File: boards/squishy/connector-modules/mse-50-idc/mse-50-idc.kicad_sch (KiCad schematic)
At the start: 14 parts, among them J1 SCSI PHY Mezz, J2 Conn_02x25_Odd_Even, J3 Conn_01x04, J4 Conn_02x34_Clockwise_Shield, J5 Conn_02x24_Clockwise_Shield, U1 M24C02-RMC

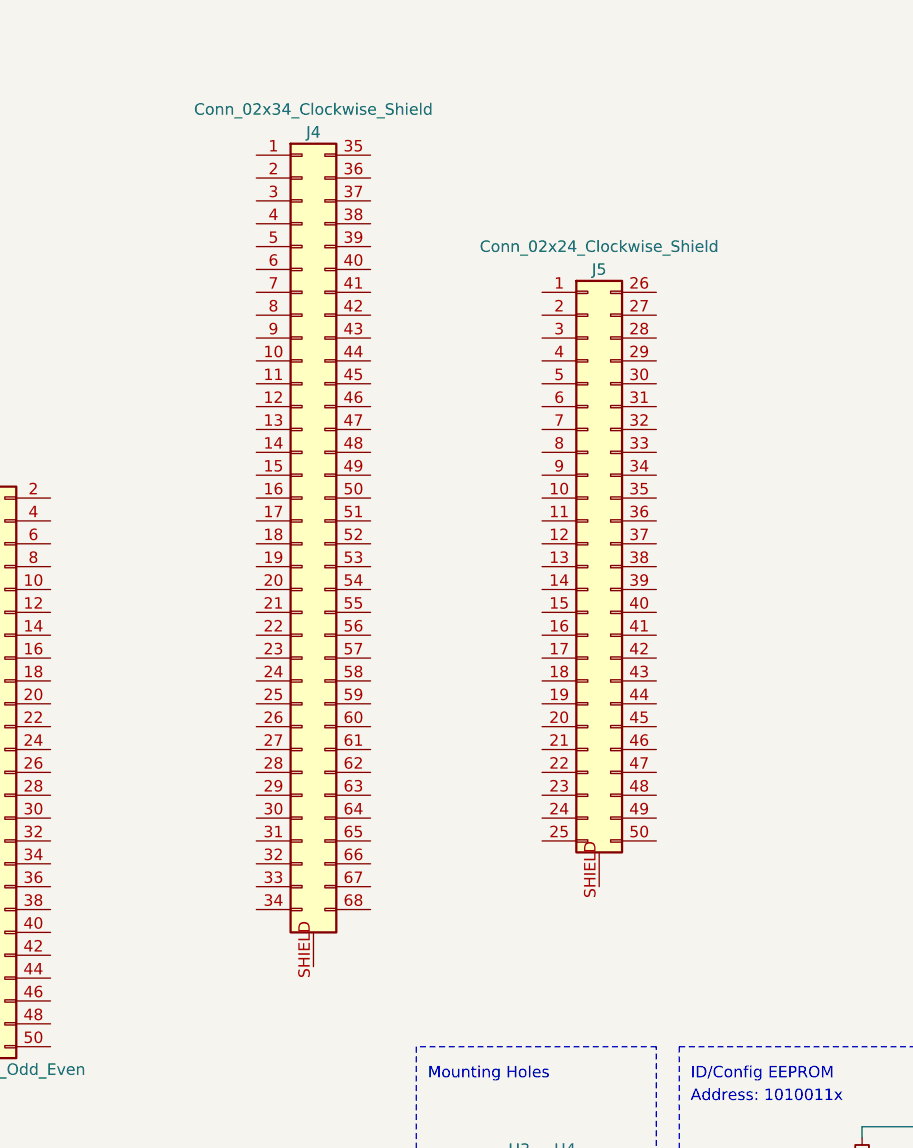
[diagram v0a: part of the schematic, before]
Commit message: squishy: connectors: Removed unneeded connector symbols in the given kicad schematics
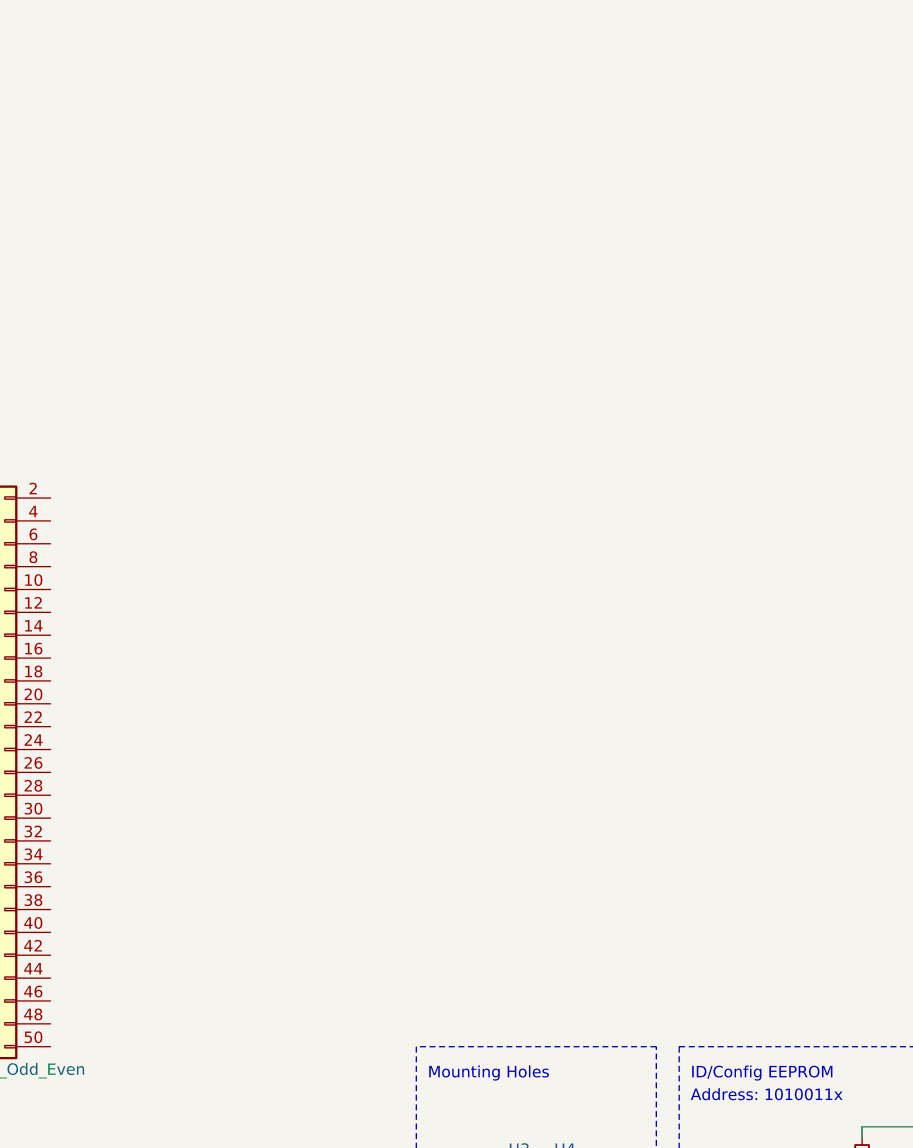
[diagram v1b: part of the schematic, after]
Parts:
- removed J4: Conn_02x34_Clockwise_Shield, symbol lethalbit-connectors:Conn_02x34_Counter_Clockwise
- removed J5: Conn_02x24_Clockwise_Shield, symbol lethalbit-connectors:Conn_02x25_Counter_Clockwise

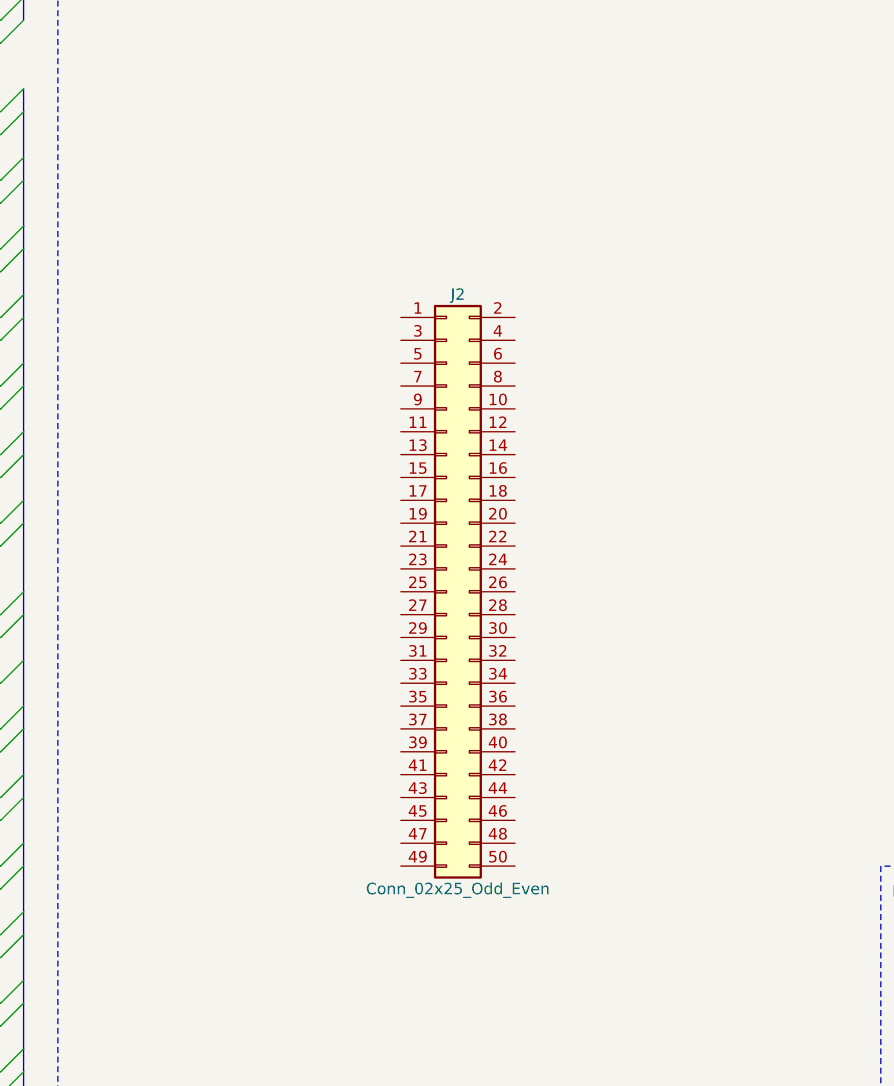
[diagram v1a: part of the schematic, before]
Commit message: squishy: connectors: hooked up mse-50-idc connector
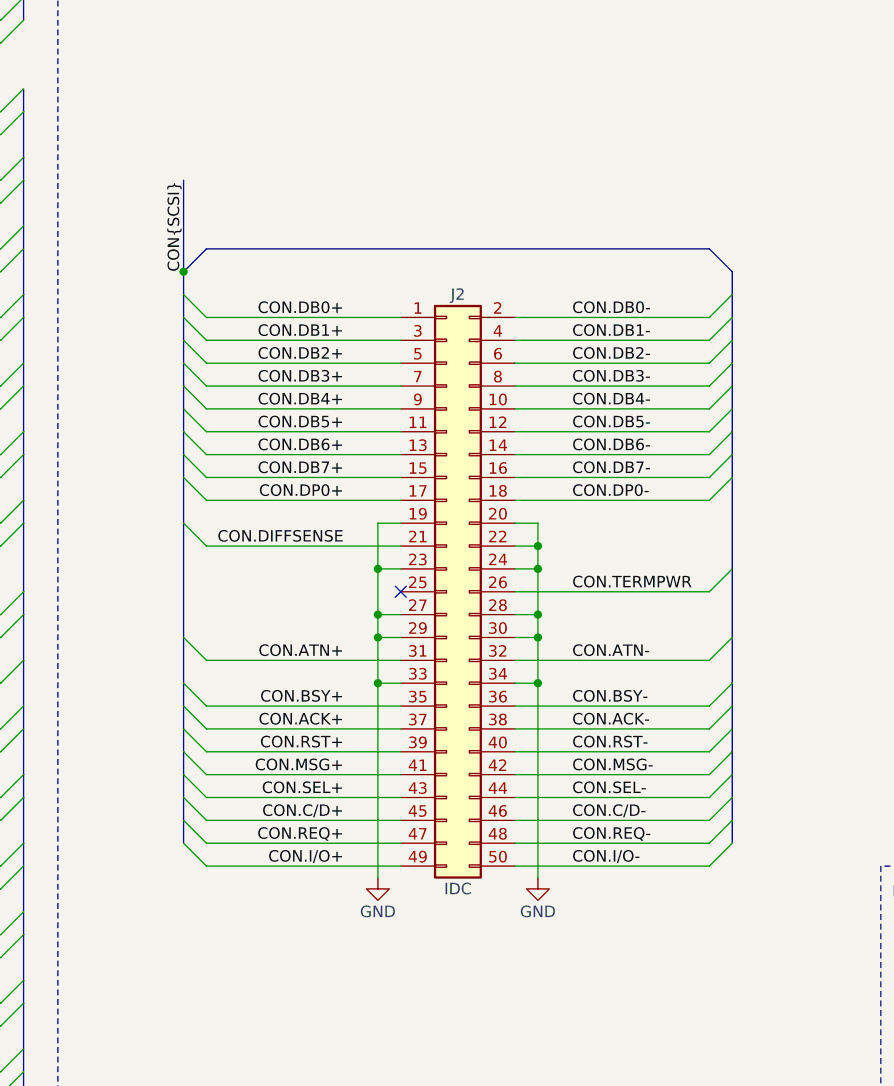
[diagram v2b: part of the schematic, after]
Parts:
- J2: value Conn_02x25_Odd_Even -> IDC
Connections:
- net CON.ACK+: now also J2.37 (Pin_37)
- net CON.ACK-: now also J2.38 (Pin_38)
- net CON.ATN+: now also J2.31 (Pin_31)
- net CON.ATN-: now also J2.32 (Pin_32)
- net CON.BSY+: now also J2.35 (Pin_35)
- net CON.BSY-: now also J2.36 (Pin_36)
- net CON.C/D+: now also J2.45 (Pin_45)
- net CON.C/D-: now also J2.46 (Pin_46)
- net CON.DB0+: now also J2.1 (Pin_1)
- net CON.DB0-: now also J2.2 (Pin_2)
- net CON.DB1+: now also J2.3 (Pin_3)
- net CON.DB1-: now also J2.4 (Pin_4)
- net CON.DB2+: now also J2.5 (Pin_5)
- net CON.DB2-: now also J2.6 (Pin_6)
- net CON.DB3+: now also J2.7 (Pin_7)
- net CON.DB3-: now also J2.8 (Pin_8)
- net CON.DB4+: now also J2.9 (Pin_9)
- net CON.DB4-: now also J2.10 (Pin_10)
- net CON.DB5+: now also J2.11 (Pin_11)
- net CON.DB5-: now also J2.12 (Pin_12)
- net CON.DB6+: now also J2.13 (Pin_13)
- net CON.DB6-: now also J2.14 (Pin_14)
- net CON.DB7+: now also J2.15 (Pin_15)
- net CON.DB7-: now also J2.16 (Pin_16)
- net CON.DIFFSENSE: now also J2.21 (Pin_21)
- net CON.DP0+: now also J2.17 (Pin_17)
- net CON.DP0-: now also J2.18 (Pin_18)
- net CON.I/O+: now also J2.49 (Pin_49)
- net CON.I/O-: now also J2.50 (Pin_50)
- net CON.MSG+: now also J2.41 (Pin_41)
- net CON.MSG-: now also J2.42 (Pin_42)
- net CON.REQ+: now also J2.47 (Pin_47)
- net CON.REQ-: now also J2.48 (Pin_48)
- net CON.RST+: now also J2.39 (Pin_39)
- net CON.RST-: now also J2.40 (Pin_40)
- net CON.SEL+: now also J2.43 (Pin_43)
- net CON.SEL-: now also J2.44 (Pin_44)
- net CON.TERMPWR: now also J2.26 (Pin_26)
- net GND: now also J2.19 (Pin_19), J2.20 (Pin_20), J2.22 (Pin_22), J2.23 (Pin_23), J2.24 (Pin_24), J2.27 (Pin_27), J2.28 (Pin_28), J2.29 (Pin_29), J2.30 (Pin_30), J2.33 (Pin_33), J2.34 (Pin_34)
- no-connect marks 2 -> 3

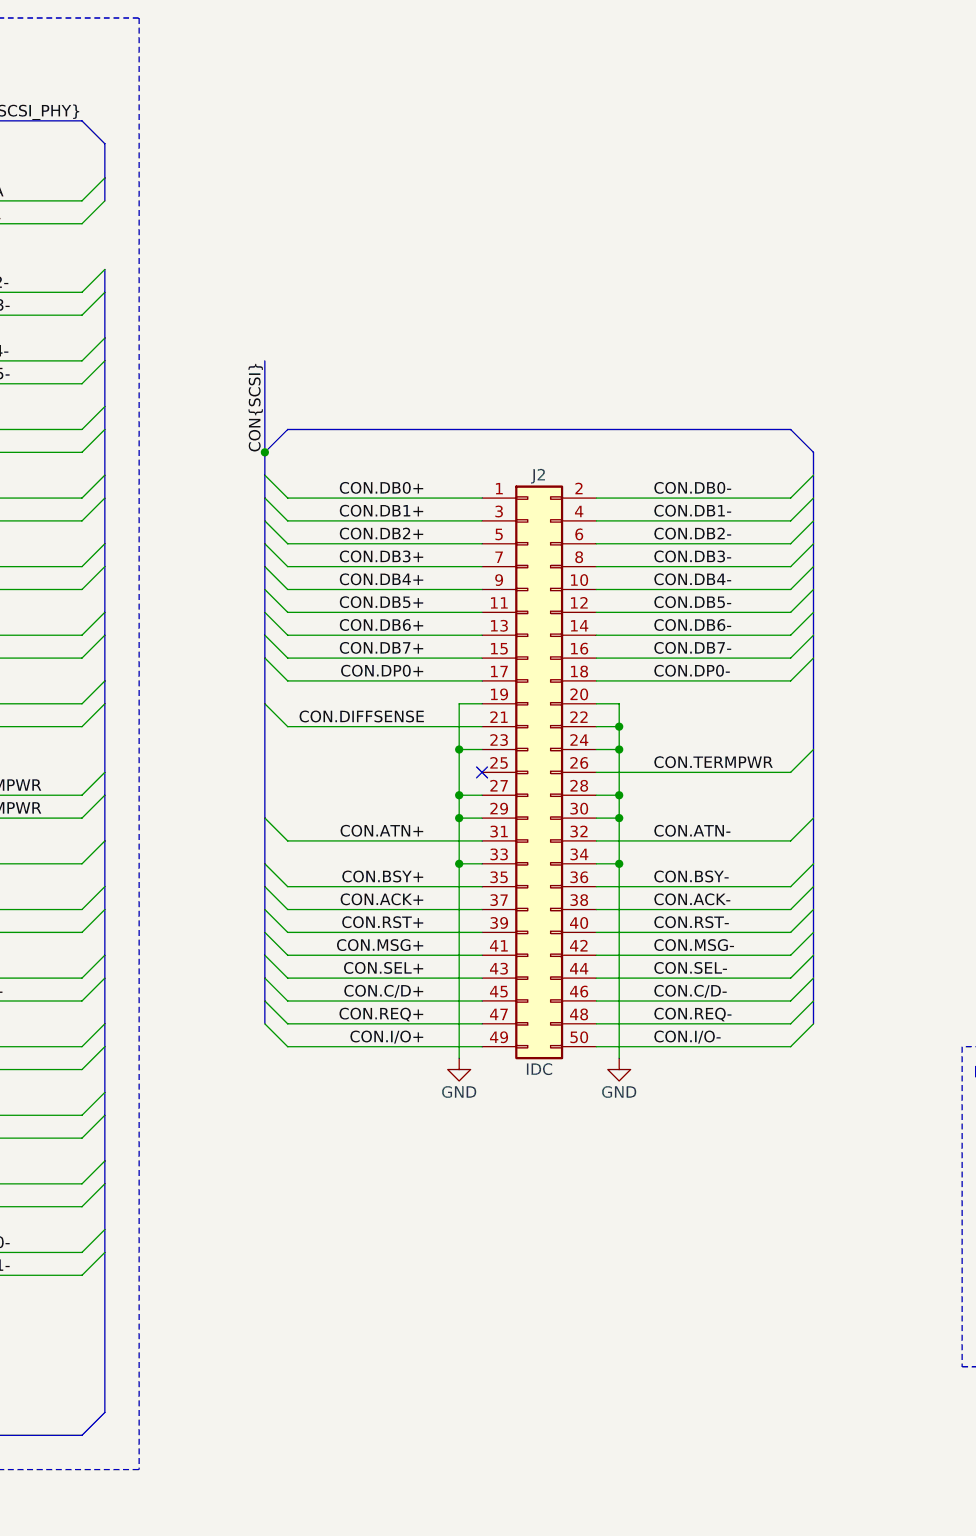
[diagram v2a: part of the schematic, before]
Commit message: squishy: connectors: Cleaned up and unified look/feel of connector schematics
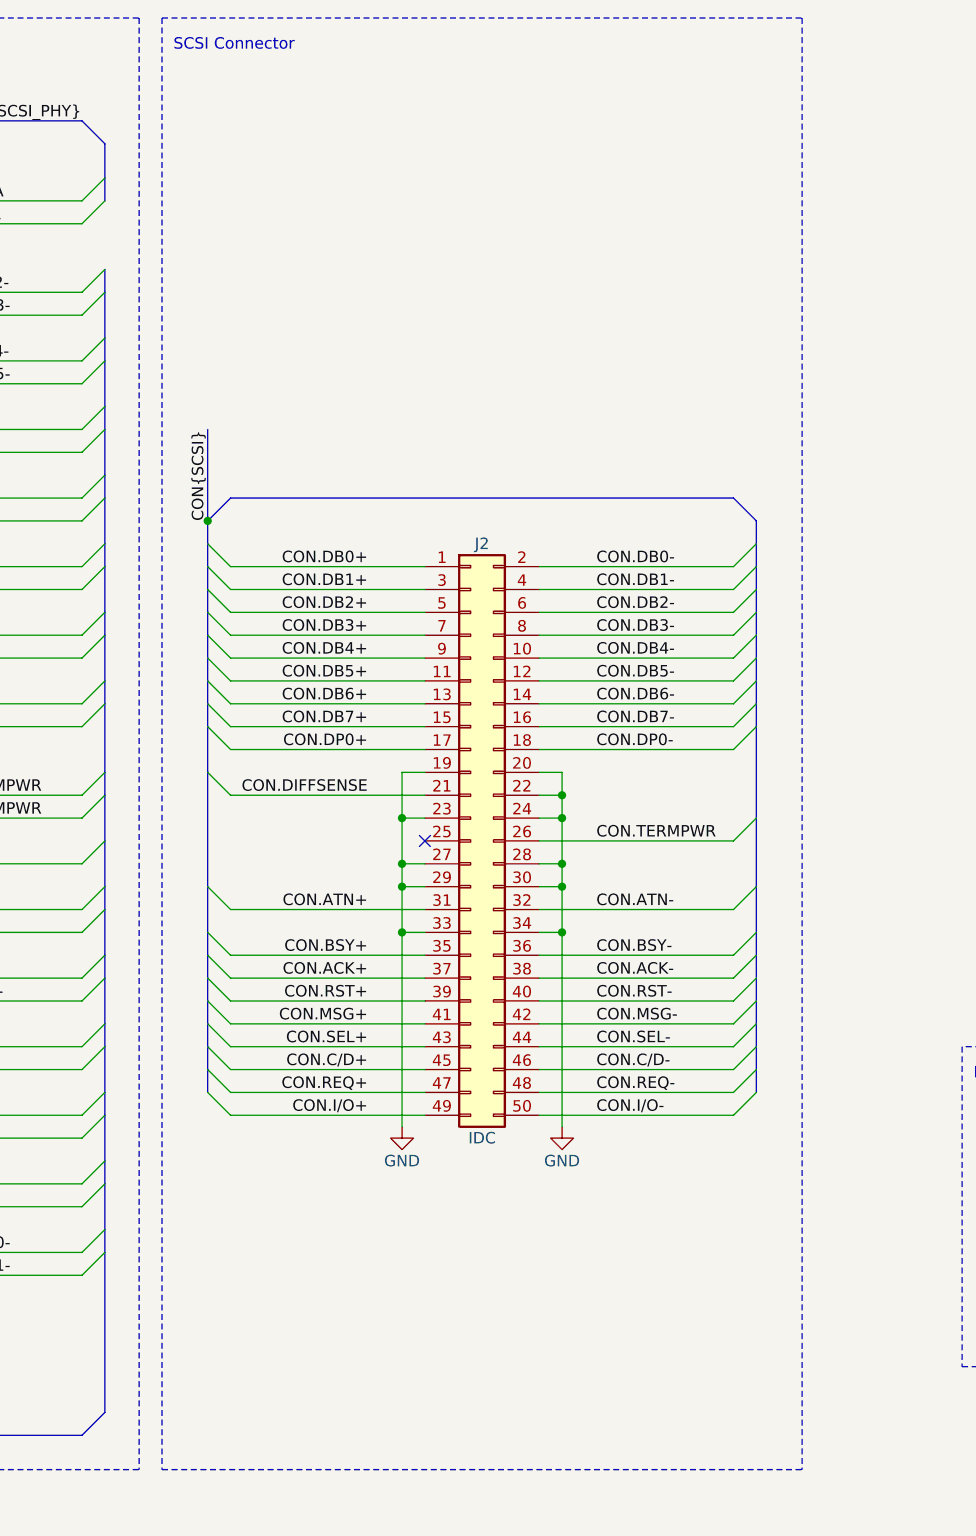
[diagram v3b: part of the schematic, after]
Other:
- note added: "SCSI Connector"
- moved on the sheet: J2

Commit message: squishy: connectors: updated schematic title blocks for connectors as appropriate
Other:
- title: Squishy -  ICD 50 -> Squishy -  SCSI LVD/MSE/SE IDC 50 Connector Module
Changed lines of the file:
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@@
 	(paper "A4")
 	(title_block
-		(title "Squishy -  ICD 50")
-		(date "2024-08-22")
+		(title "Squishy -  SCSI LVD/MSE/SE IDC 50 Connector Module")
+		(date "2024-09-17")
 		(rev "1")
 		(company "Shrine Maiden Heavy Industries")

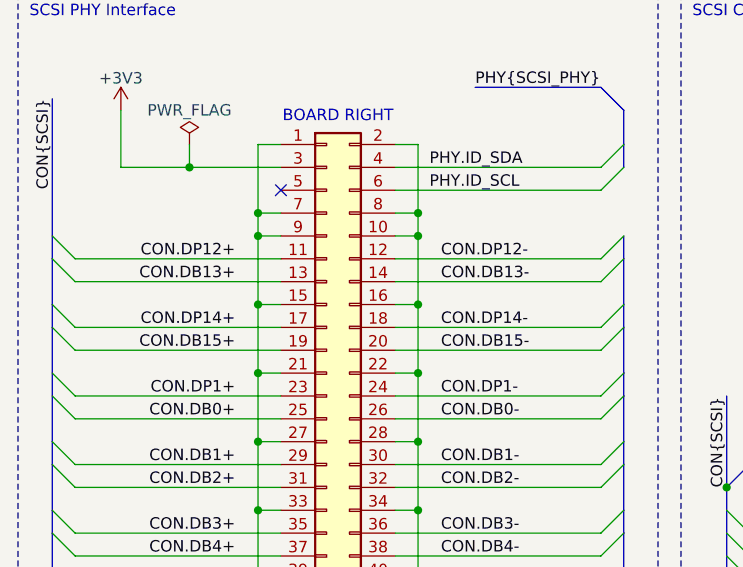
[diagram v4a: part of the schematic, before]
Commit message: squishy: connectors: s/DP12/DB12/g s/DP14/DB14/g
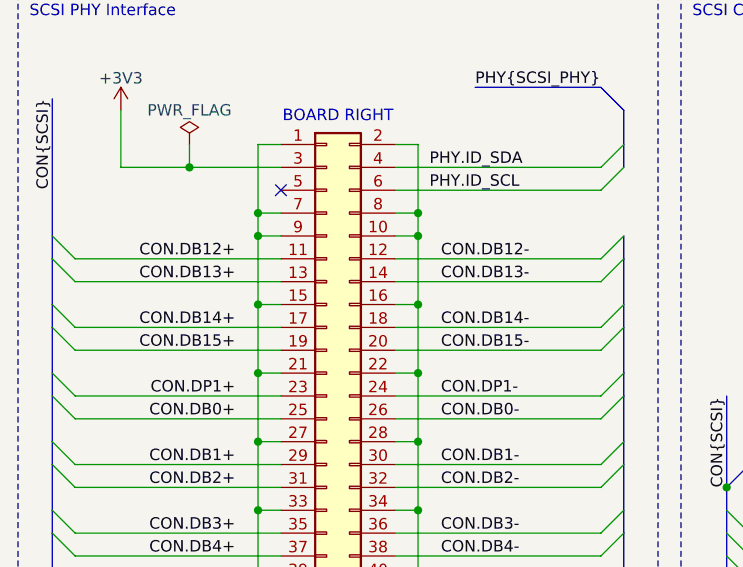
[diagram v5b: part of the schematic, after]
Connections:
- net CON.DP12+ renamed CON.DB12+
- net CON.DP12- renamed CON.DB12-
- net CON.DP14+ renamed CON.DB14+
- net CON.DP14- renamed CON.DB14-
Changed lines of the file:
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@@
 		)
 	)
-	(label "CON.DP14-"
+	(label "CON.DB14-"
 		(at 60.96 52.07 0)
 		(fields_autoplaced yes)
@@
 		)
 	)
-	(label "CON.DP12+"
+	(label "CON.DB12+"
 		(at 38.1 44.45 180)
 		(fields_autoplaced yes)
@@
 		)
 	)
-	(label "CON.DP12-"
+	(label "CON.DB12-"
 		(at 60.96 44.45 0)
 		(fields_autoplaced yes)
@@
 		)
 	)
-	(label "CON.DP14+"
+	(label "CON.DB14+"
 		(at 38.1 52.07 180)
 		(fields_autoplaced yes)

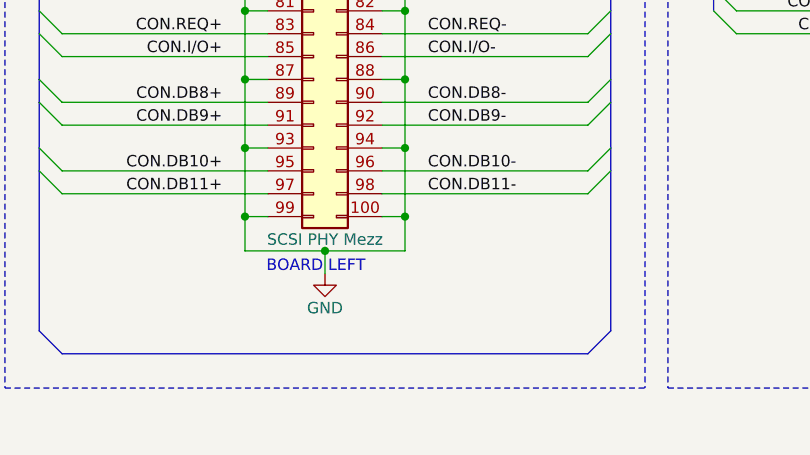
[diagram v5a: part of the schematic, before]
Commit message: squishy: connectors: cleaned up ERC on the mse-50-idc connector
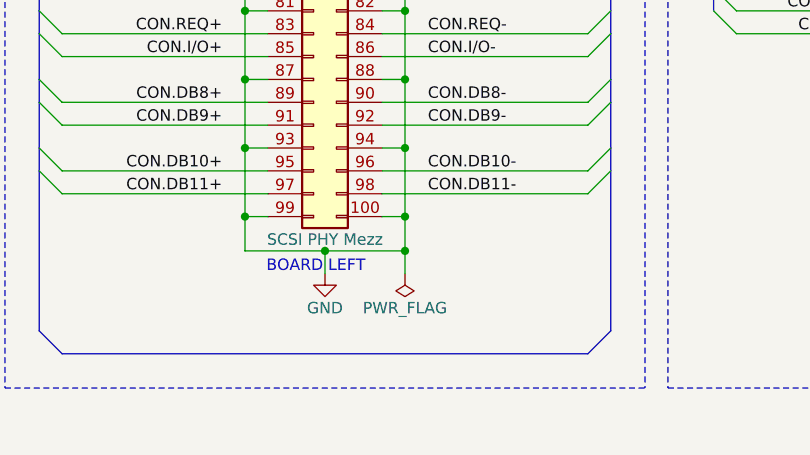
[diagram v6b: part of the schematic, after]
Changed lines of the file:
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@@
 	)
 	(junction
+		(at 58.42 160.02)
+		(diameter 0)
+		(color 0 0 0 0)
+	)
+	(junction
 		(at 114.3 107.95)
 		(diameter 0)
@@
 	(wire
 		(pts
+			(xy 58.42 160.02) (xy 58.42 162.56)
+		)
+		(stroke
+			(width 0)
+			(type default)
+		)
+	)
+	(wire
+		(pts
 			(xy 20.32 44.45) (xy 43.18 44.45)
 		)
@@
 					(unit 1)
 				)
+			)
+		)
+	)
+	(symbol
+		(lib_id "power:PWR_FLAG")
+		(at 58.42 162.56 180)
+		(unit 1)
+		(exclude_from_sim no)
+		(in_bom yes)
+		(on_board yes)
+		(dnp no)
+		(property "Reference" "#FLG02"
+			(at 58.42 164.465 0)
+			(effects
+				(font
+					(size 1.27 1.27)
+				)
+				(hide yes)
+			)
+		)
+		(property "Value" "PWR_FLAG"
+			(at 58.42 166.37 0)
+			(effects
+				(font
+					(size 1.27 1.27)
+				)
+			)
+		)
+		(property "Footprint" ""
+			(at 58.42 162.56 0)
+			(effects
+				(font
+					(size 1.27 1.27)
+				)
+				(hide yes)
+			)
+		)
+		(property "Datasheet" "~"
+			(at 58.42 162.56 0)
+			(effects
+				(font
+					(size 1.27 1.27)
+				)
+				(hide yes)
+			)
+		)
+		(property "Description" "Special symbol for telling ERC where power comes from"
+			(at 58.42 162.56 0)
+			(effects
+				(font
+					(size 1.27 1.27)
+				)
+				(hide yes)
+			)
+		)
+		(pin "1"
+		)
+		(instances
+			(project "mse-50-idc"
+				(path "/bd9eafec-5355-49e4-b2e3-916daacb0a86"
+					(reference "#FLG02")
+					(unit 1)
+				)
